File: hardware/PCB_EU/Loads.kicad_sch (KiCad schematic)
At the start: 15 parts, among them J701 PTC + / RETURN, J702 PUMP + / RETURN, Q701 BC847B-DIO, Q702 BC857B, Q703 IRF1010ESPBF, Q704 AO3422

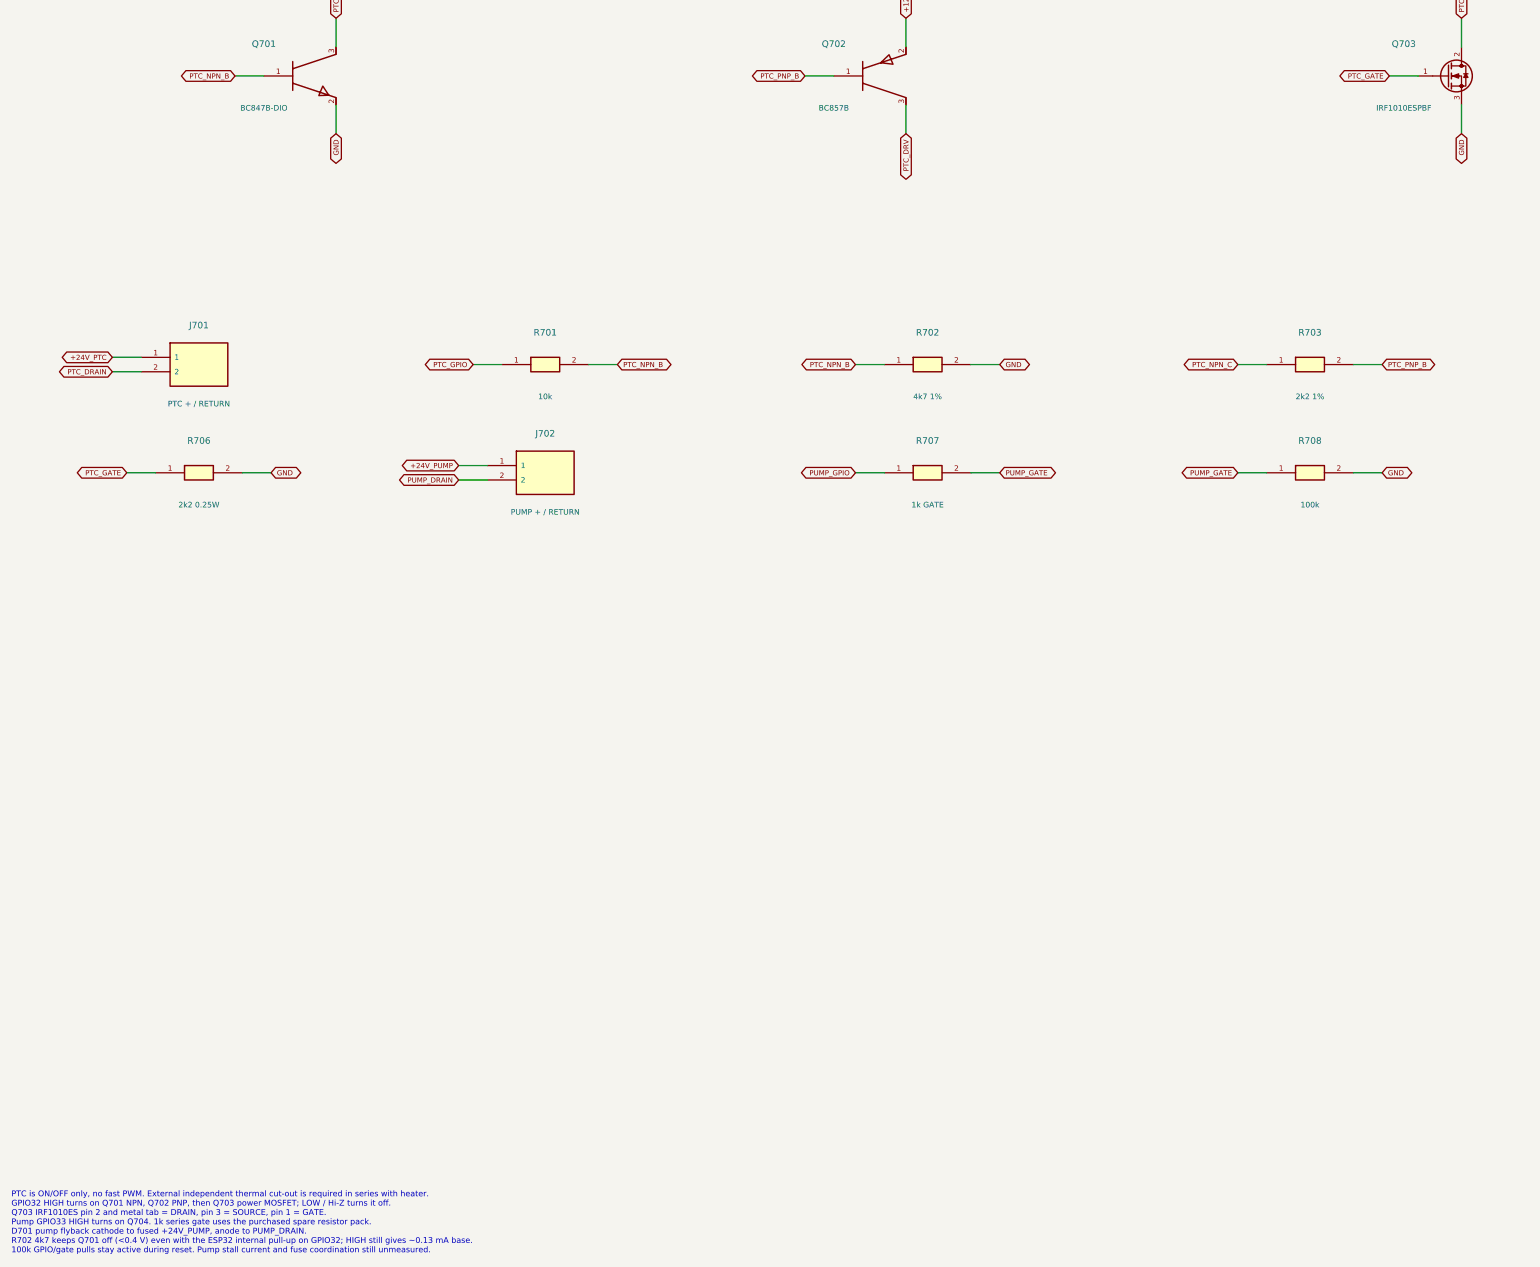
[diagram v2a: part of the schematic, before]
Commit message: PCB_EU: Q601 CSD19534KCS, Q102/Q703 FDB5800, BOM updated
Q601 (LED2 boost switch, no heatsink): TK22E10N1 -> TI CSD19534KCS on the
same TO-220 land. Q102 (reverse polarity) and Q703 (PTC switch):
IRF1010ESPBF -> onsemi FDB5800 on the same TO-263-2 land. Q501 stays
TK22E10N1.

BOM 82.50 -> 85.75 EUR: FDB5800 x2 Salvats 3.96 (was IRF 2.42),
TK22E10N1 x1 instead of x2 (-1.38), CSD19534KCS x1 Electrobase 3.09.
Shipping 5.87 and the two parcels are unchanged.

tools/generate.py rebuilds schematics, design.json and the BOM (the
generator is idempotent). Value/Datasheet/MPN/Design_note of the three
parts are text-patched in PCB_EU.kicad_pcb and review/netlist.xml the way
a KiCad export and build_board.py would write them; review/connectivity.txt
comes from tools/verify.py (56 checks pass). DESIGN.md and README.md are
updated.

KiCad was not run: ERC, DRC, schematic parity and the other KiCad-based
checks of run_checks.py have NOT been run for this commit.

Co-Authored-By: Claude Sonnet 5.5 <noreply@anthropic.com>
Claude-Session: https://claude.ai/code/session_011GxPyRnAFpBjFQ5VURqV5H
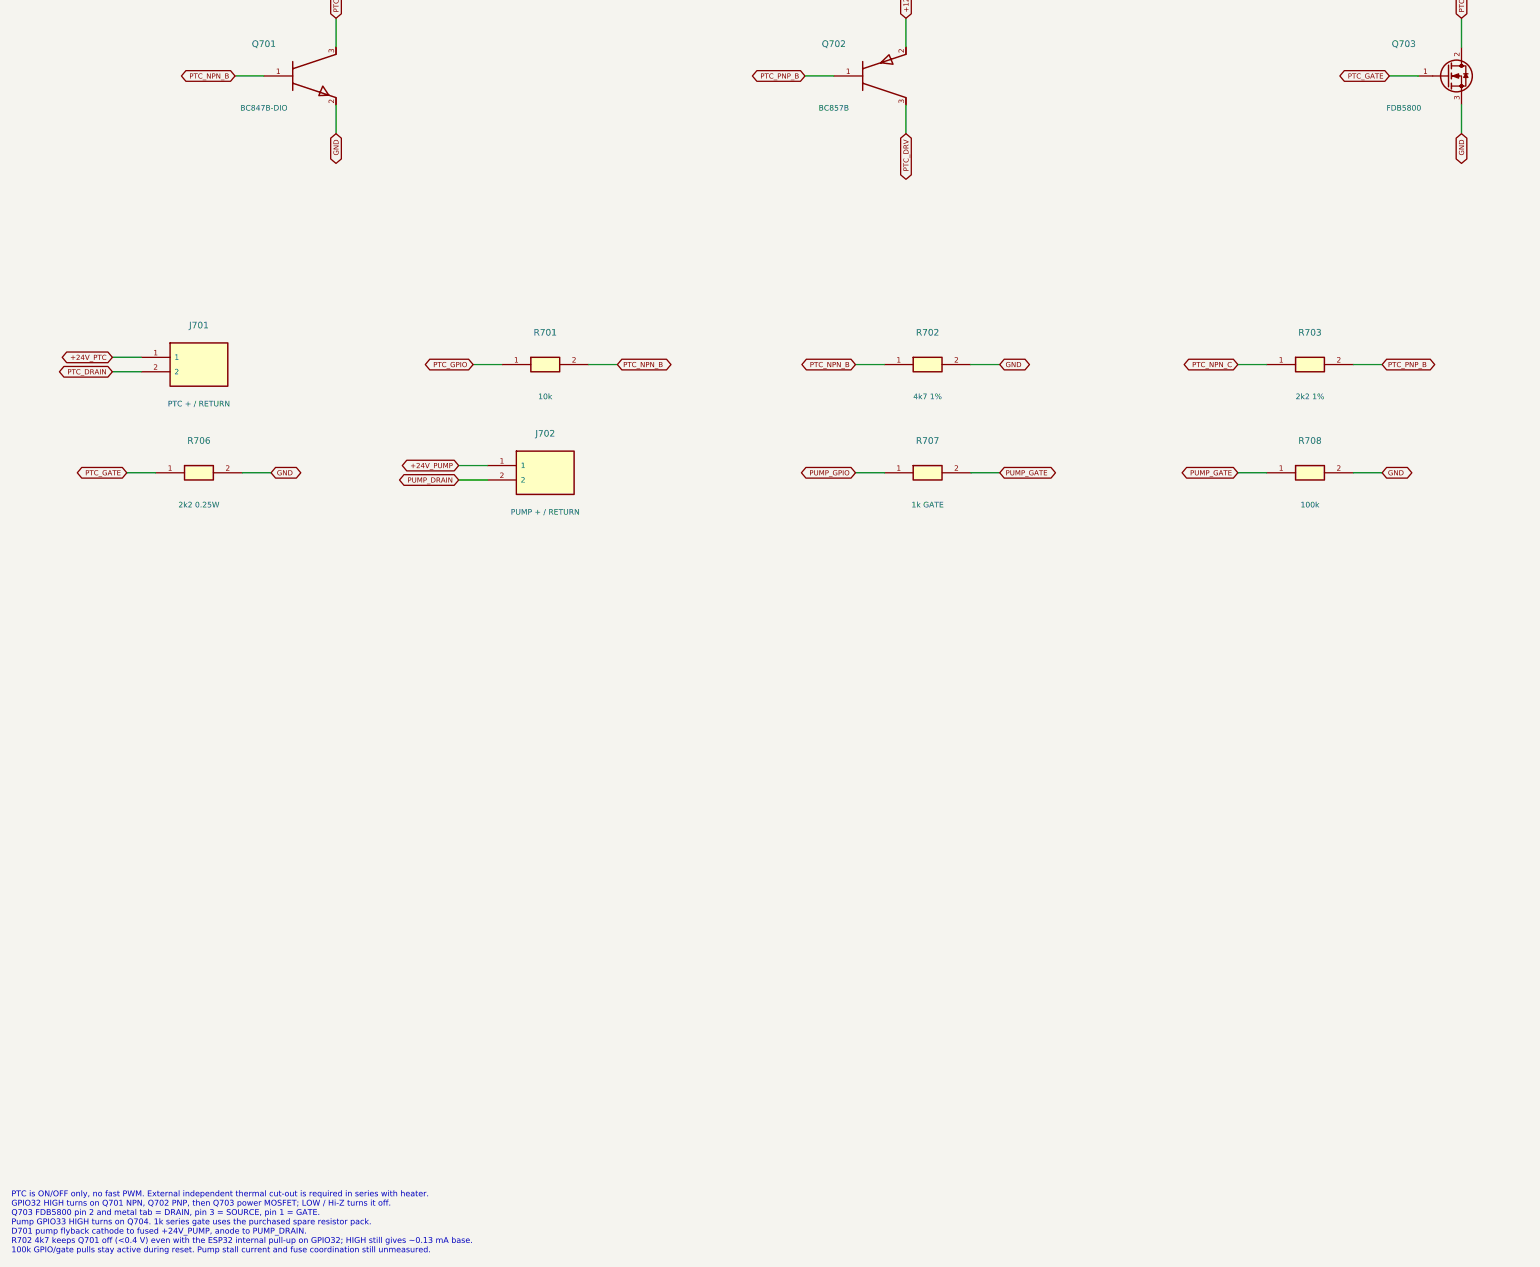
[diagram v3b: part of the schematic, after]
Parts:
- Q703: value IRF1010ESPBF -> FDB5800; MPN IRF1010ESPBF -> FDB5800
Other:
- note added: "PTC is ON/OFF only, no fast PWM. External independent thermal cut-out is required in series with heater. GPIO32 HIGH turns on Q701 NPN, Q702 PNP, then Q703 power MOSFET; LOW / Hi-Z turns it off. Q703 FDB5800 pin 2 and metal tab = DRAIN, pin 3 = SOURCE, pin 1 = GATE. Pump GPIO33 HIGH turns on Q704. 1k series gate uses the purchased spare resistor pack. D701 pump flyback cathode to fused +24V_PUMP,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"
- note removed: "PTC is ON/OFF only, no fast PWM. External independent thermal cut-out is required in series with heater. GPIO32 HIGH turns on Q701 NPN, Q702 PNP, then Q703 power MOSFET; LOW / Hi-Z turns it off. Q703 IRF1010ES pin 2 and metal tab = DRAIN, pin 3 = SOURCE, pin 1 = GATE. Pump GPIO33 HIGH turns on Q704. 1k series gate uses the purchased spare resistor pack. D701 pump flyback cathode to fused +24V_PUM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"
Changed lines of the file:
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@@
 (kicad_sch (version 20260306) (generator "eeschema") (generator_version "10.0") (paper "A3") (title_block (title "07 | PTC heater and 24 V pump") (date "2026-10-20") (rev "EU-0.1") (company "GrowBox | EU prototype") (comment 1 "SCHEMATIC DRAFT | PARTIAL LED1 PCB ROUTING | no manufacturing release"))
 (text "07 | PTC heater and 24 V pump" (at 12.7 12.7 0) (effects (font (size 2 2)) (justify left top)))
-(text "PTC is ON/OFF only, no fast PWM. External independent thermal cut-out is required in series with heater.\nGPIO32 HIGH turns on Q701 NPN, Q702 PNP, then Q703 power MOSFET; LOW / Hi-Z turns it off.\nQ703 IRF1010ES pin 2 and metal tab = DRAIN, pin 3 = SOURCE, pin 1 = GATE.\nPump GPIO33 HIGH turns on Q704. 1k series gate uses the purchased spare resistor pack.\nD701 pump flyback cathode to fused +24V_PUMP, anode to PUMP_DRAIN.\nR702 4k7 keeps Q701 off (<0.4 V) even with the ESP32 internal pull-up on GPIO32; HIGH still gives ~0.13 mA base.\n100k GPIO/gate pulls stay active during reset. Pump stall current and fuse coordination still unmeasured." (at 12.7 251 0) (effects (font (size 1.02 1.02)) (justify left top)))
+(text "PTC is ON/OFF only, no fast PWM. External independent thermal cut-out is required in series with heater.\nGPIO32 HIGH turns on Q701 NPN, Q702 PNP, then Q703 power MOSFET; LOW / Hi-Z turns it off.\nQ703 FDB5800 pin 2 and metal tab = DRAIN, pin 3 = SOURCE, pin 1 = GATE.\nPump GPIO33 HIGH turns on Q704. 1k series gate uses the purchased spare resistor pack.\nD701 pump flyback cathode to fused +24V_PUMP, anode to PUMP_DRAIN.\nR702 4k7 keeps Q701 off (<0.4 V) even with the ESP32 internal pull-up on GPIO32; HIGH still gives ~0.13 mA base.\n100k GPIO/gate pulls stay active during reset. Pump stall current and fuse coordination still unmeasured." (at 12.7 251 0) (effects (font (size 1.02 1.02)) (justify left top)))
 (symbol (lib_id "EU:J2") (at 45.72 105.41 0) (unit 1) (in_bom yes) (on_board yes) (dnp no)
 (property "Reference" "J701" (at 45.72 98.5 0) (effects (font (size 1.15 1.15)) ))
@@
 (symbol (lib_id "EU:NMOS") (at 265.43 54.61 0) (unit 1) (in_bom yes) (on_board yes) (dnp no)
 (property "Reference" "Q703" (at 257.81 48.97 0) (effects (font (size 1.15 1.15)) ))
-(property "Value" "IRF1010ESPBF" (at 257.81 60.25 0) (effects (font (size 0.98 0.98)) ))
+(property "Value" "FDB5800" (at 257.81 60.25 0) (effects (font (size 0.98 0.98)) ))
 (property "Footprint" "Package_TO_SOT_SMD:TO-263-2" (at 265.43 54.61 0) (effects (font (size 1 1)) (hide yes)))
-(property "Datasheet" "" (at 265.43 54.61 0) (effects (font (size 1 1)) (hide yes)))
-(property "MPN" "IRF1010ESPBF" (at 265.43 54.61 0) (effects (font (size 1 1)) (hide yes)))
+(property "Datasheet" "https://www.onsemi.com/pdf/datasheet/fdb5800-d.pdf" (at 265.43 54.61 0) (effects (font (size 1 1)) (hide yes)))
+(property "MPN" "FDB5800" (at 265.43 54.61 0) (effects (font (size 1 1)) (hide yes)))
 (property "Design_note" "" (at 265.43 54.61 0) (effects (font (size 1 1)) (hide yes)))
 (property "FootprintStatus" "PACKAGE ONLY - verify before PCB" (at 265.43 54.61 0) (effects (font (size 1 1)) (hide yes)))
